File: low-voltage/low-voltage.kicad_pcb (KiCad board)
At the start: 2 copper layers, 124 x 101 mm, 34 parts, among them J1 Conn_Coaxial, J2 Conn_01x01, J3 Conn_01x01, J4 Conn_01x01, Q1 2N4401, SW1 SW_SPST, SW2 SW_SPDT, U1 NJM2113

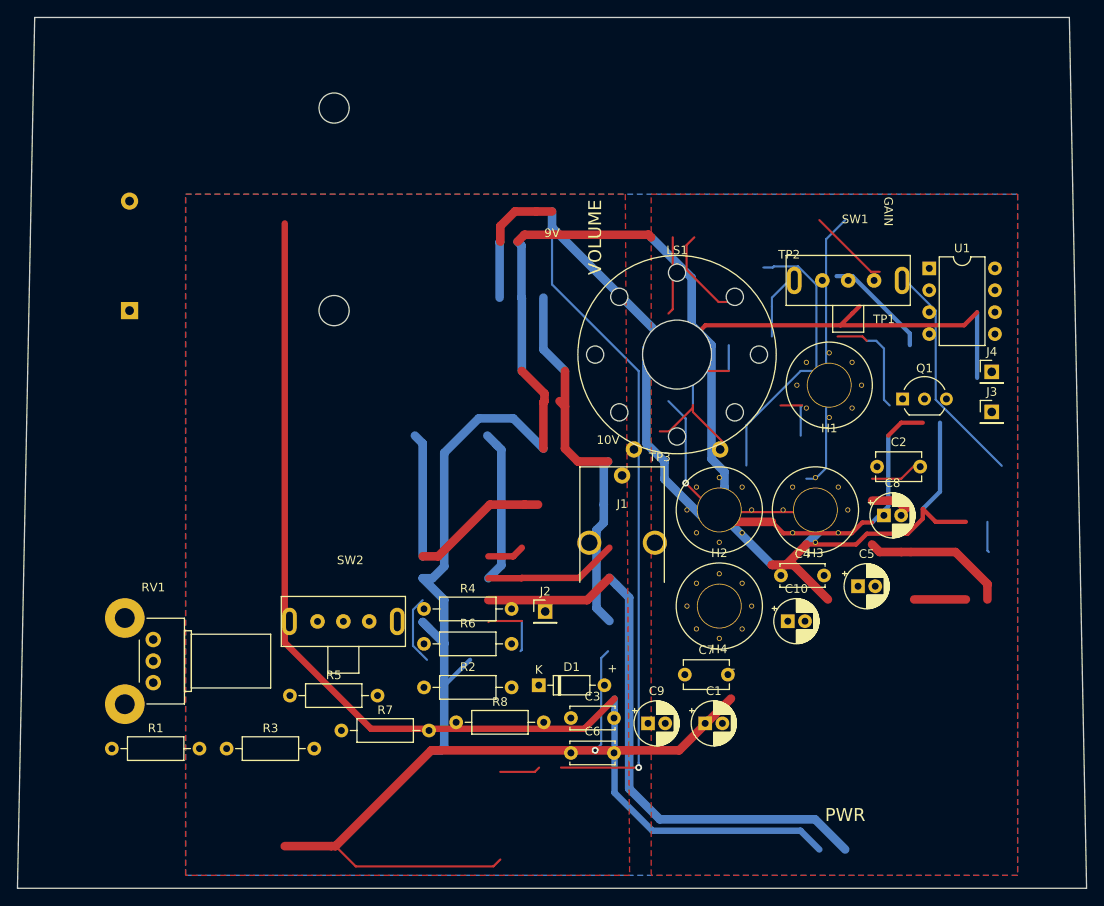
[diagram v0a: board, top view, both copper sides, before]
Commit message: Place components for low voltage
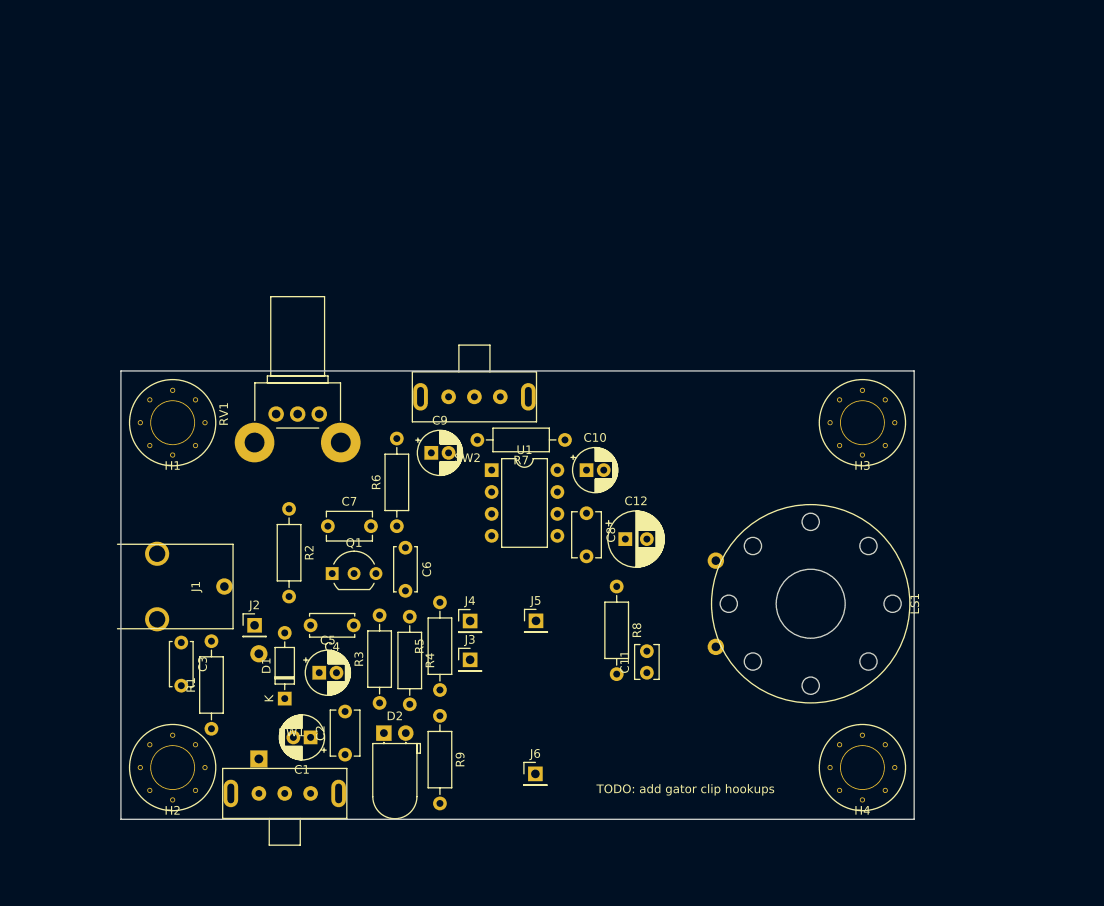
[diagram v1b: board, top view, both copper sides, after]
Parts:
- added C11: 47000pF, Capacitor_THT:C_Disc_D3.8mm_W2.6mm_P2.50mm, F.Cu at (136.0, 93.0)
- added C12: 220uF, Capacitor_THT:CP_Radial_D6.3mm_P2.50mm, F.Cu at (133.5, 77.5)
- added D2: LED, LED_THT:LED_D5.0mm_Horizontal_O1.27mm_Z9.0mm, F.Cu at (105.5, 100.0)
- added J5: Conn_01x01, Connector_PinHeader_2.54mm:PinHeader_1x01_P2.54mm_Vertical, F.Cu at (123.1, 87.0)
- added J6: Conn_01x01, Connector_PinHeader_2.54mm:PinHeader_1x01_P2.54mm_Vertical, F.Cu at (123.1, 104.7)
- added R9: 10k, Resistor_THT:R_Axial_DIN0207_L6.3mm_D2.5mm_P10.16mm_Horizontal, F.Cu at (112.0, 98.0)
- BT1: footprint Battery:BatteryHolder_Keystone_2479_3xAAA -> homebrew:BatteryHolder_Keystone_2481_4xAAA
- C8: value 1uF -> 0.1uF; footprint Capacitor_THT:CP_Radial_D5.0mm_P2.00mm -> Capacitor_THT:C_Disc_D5.1mm_W3.2mm_P5.00mm
- R2, R5: value 10M -> 1M
- R4: value 47k -> 22k
- R7: value 47k -> 1.3k
- R8: value 22k -> 10
- SW2: value SW_SPDT -> SW_SPST
- U1: value NJM2113 -> LM386
- moved SW1 88.4 mm to (94.0, 107.0)
- moved H1 76.3 mm to (81.0, 64.0)
- moved C2 70.2 mm to (101.0, 102.5), turned to 90 degrees
- moved H2 70.1 mm to (81.0, 104.0)
- moved Q1 69.2 mm to (99.5, 81.5)
- moved J4 67.0 mm to (115.5, 87.0)
- moved J3 67.0 mm to (115.5, 91.5)
- moved C5 63.3 mm to (98.0, 93.0)
- moved U1 55.9 mm to (118.0, 69.5)
- moved BT1 54.1 mm to (91.0, 103.0)
- moved C4 49.9 mm to (102.0, 87.5), turned to 180 degrees
- moved J1 47.9 mm to (87.0, 83.0), turned to 270 degrees
- moved C3 46.0 mm to (82.0, 89.5), turned to 270 degrees
- moved C1 45.8 mm to (97.0, 100.5), turned to 180 degrees
- moved C7 44.8 mm to (99.0, 76.0)
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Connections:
- net Net-(BT1-Pad1) renamed /BAT+
- C10 pad 1: VCC -> Net-(C10-Pad1)
- C8 pad 1: Net-(C8-Pad1) -> VCC
- C9 pad 2: GND -> Net-(C9-Pad2)
- LS1 pad 1: Net-(LS1-Pad1) -> Net-(C12-Pad2)
- LS1 pad 2: Net-(LS1-Pad2) -> GND
- R7 pad 2: SIGNAL -> Net-(C9-Pad2)
- R8 pad 1: SIGNAL -> Net-(C12-Pad1)
- R8 pad 2: Net-(R8-Pad2) -> Net-(C11-Pad1)
- RV1 pad 1: Net-(C7-Pad1) -> GND
- RV1 pad 3: GND -> Net-(C7-Pad1)
- SW2 pad 1: Net-(R8-Pad2) -> Net-(SW2-Pad1)
- SW2 pad 2: Net-(LS1-Pad1) -> Net-(C9-Pad1)
- SW2 pad 3: Net-(R7-Pad1) -> (no net)
- U1 pad 1: GND -> Net-(SW2-Pad1)
- U1 pad 2: Net-(C9-Pad1) -> GND
- U1 pad 3: Net-(C8-Pad1) -> SIGNAL
- U1 pad 4: SIGNAL -> GND
- U1 pad 5: Net-(LS1-Pad1) -> Net-(C12-Pad1)
- U1 pad 7: GND -> Net-(C10-Pad1)
- U1 pad 8: Net-(LS1-Pad2) -> Net-(R7-Pad1)
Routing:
- net (no net): track 344.8 -> 0.00 mm, vias 3 -> 0
- net GND: track 228.7 -> 0.00 mm, vias 1 -> 0
- net SIGNAL: track 92.5 -> 0.00 mm
- net Net-(R1-Pad2): track 68.5 -> 0.00 mm
- net /10v: track 44.7 -> 0.00 mm
- net Net-(A1-Pad1): track 37.4 -> 0.00 mm
- net /audio-rf/TP2: track 35.3 -> 0.00 mm
- net Net-(L1-Pad1): track 33.3 -> 0.00 mm
- net Net-(D1-Pad2): track 30.2 -> 0.00 mm
- net Net-(C13-Pad2): track 27.5 -> 0.00 mm
- net +9V: track 25.9 -> 0.00 mm
- net Net-(C15-Pad1): track 17.1 -> 0.00 mm
- net /audio-rf/TP1: track 12.8 -> 0.00 mm
- net VCC: track 12.6 -> 0.00 mm
- net Net-(LS1-Pad2): track 11.2 -> 0.00 mm
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- removed copper zone on F.Cu, net +9V
- removed copper zone on B.Cu, net GND
- removed copper zone on F.Cu, net Net-(A1-Pad1)
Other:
- board size 124 x 101 mm -> 92 x 52 mm
- board text added: "TODO: add gator clip hookups"
- board text removed: "+"
- board text removed: "-"
- board text removed: "10V"
- board text removed: "9V"
- board text removed: "GAIN"
- board text removed: "PWR"
- board text removed: "TP1"
- board text removed: "TP2"
- board text removed: "TP3"
- board text removed: "VOLUME"

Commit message: Final design for low voltage (v2.0)
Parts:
- added C13: 220uF, Capacitor_THT:CP_Radial_D6.3mm_P2.50mm, F.Cu at (118.0, 99.0)
- added G***: OSHW_LOGO_4mm, homebrew:OSHW_LOGO_4mm, F.Cu at (151.0, 66.5)
- J5, J6: footprint Connector_PinHeader_2.54mm:PinHeader_1x01_P2.54mm_Vertical -> homebrew:ALLIGATOR_CLIP_SLOT
- moved J5 19.9 mm to (119.5, 106.5)
- moved J6 13.1 mm to (136.0, 106.5)
- moved J4 6.52 mm to (112.0, 81.5)
- moved R1 1.00 mm to (86.5, 99.5)
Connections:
- J5 pad 1: /BAT+ -> VCC
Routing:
- net GND: track 0.00 -> 200.3 mm, vias 0 -> 5
- net VCC: track 0.00 -> 100.6 mm, vias 0 -> 1
- net /TP3: track 0.00 -> 36.7 mm
- net Net-(R2-Pad1): track 0.00 -> 24.4 mm, vias 0 -> 1
- net /TP2: track 0.00 -> 20.3 mm
- net Net-(C3-Pad2): track 0.00 -> 16.9 mm
- net Net-(C7-Pad1): track 0.00 -> 15.5 mm
- net Net-(C12-Pad1): track 0.00 -> 14.0 mm
- net Net-(R6-Pad2): track 0.00 -> 13.8 mm
- net /TP1: track 0.00 -> 11.7 mm
- net SIGNAL: track 0.00 -> 11.6 mm
- net Net-(C12-Pad2): track 0.00 -> 9.04 mm
- net Net-(SW2-Pad1): track 0.00 -> 8.91 mm
- net Net-(C9-Pad1): track 0.00 -> 8.57 mm
- net Net-(C3-Pad1): track 0.00 -> 8.57 mm
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- added copper zone on B.Cu, net GND
- added copper zone on F.Cu, net GND
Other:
- board text added: "+"
- board text added: "-"
- board text added: "HI GAIN"
- board text added: "LO"
- board text added: "PWR"
- board text added: "TP1"
- board text added: "TP2"
- board text added: "TP3"
- board text added: "VOL"
- board text added: "all-band receiver v2.0"
- board text removed: "TODO: add gator clip hookups"
